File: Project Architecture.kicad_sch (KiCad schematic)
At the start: 0 parts

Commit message: First draft of schematic
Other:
- sheet Section A - Title A renamed SolarCharger
- sheet Section B - Title B renamed MCU
- added sheet Connectors (connectors.kicad_sch)
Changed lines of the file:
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@@
+	)
+	(sheet
+		(at 190.5 152.4)
+		(size 39.37 21.59)
+		(exclude_from_sim no)
+		(in_bom yes)
+		(on_board yes)
+		(dnp no)
+		(fields_autoplaced yes)
+		(stroke
+			(width 0.1524)
+			(type solid)
+		)
+		(fill
+			(color 0 0 0 0.0000)
+		)
+		(property "Sheetname" "Connectors"
+			(at 190.5 151.6884 0)
+			(effects
+				(font
+					(size 1.27 1.27)
+				)
+				(justify left bottom)
+			)
+		)
+		(property "Sheetfile" "connectors.kicad_sch"
+			(at 190.5 174.5746 0)
+			(effects
+				(font
+					(size 1.27 1.27)
+				)
+				(justify left top)
+			)
+		)
+		(instances
+			(project "solar_smart_station"
+				(path "/f9e05184-c88b-4a88-ae9c-ab2bdb32be7c/c5103ceb-5325-4a84-a025-9638a412984e"
+					(page "6")
+				)
+			)
+		)
 	)
 	(sheet
@@
 			(color 255 200 0 0.5020)
 		)
-		(property "Sheetname" "Section B - Title B"
+		(property "Sheetname" "MCU"
 			(at 190.5 113.2709 0)
 			(effects
@@
 			(color 128 255 128 0.5000)
 		)
-		(property "Sheetname" "Section A - Title A"
+		(property "Sheetname" "SolarCharger"
 			(at 190.5 75.1709 0)
 			(effects

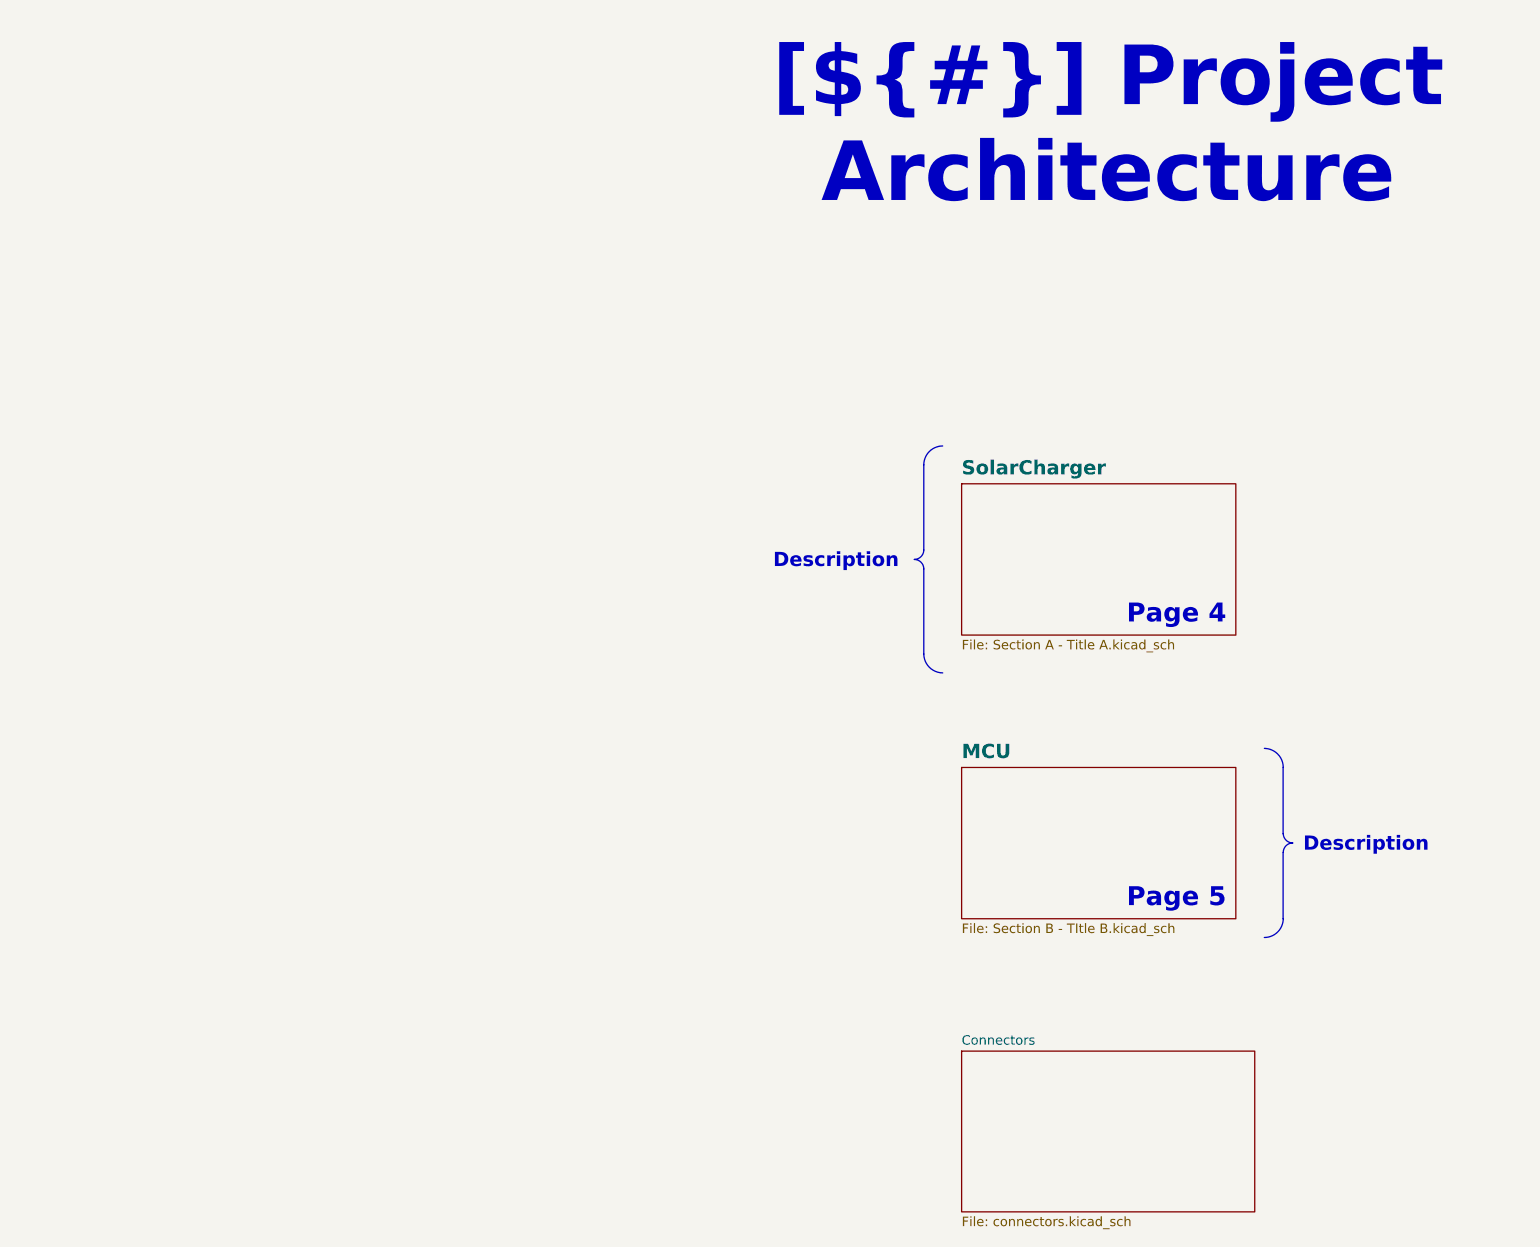
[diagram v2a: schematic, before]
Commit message: Add cell balancer - in progress
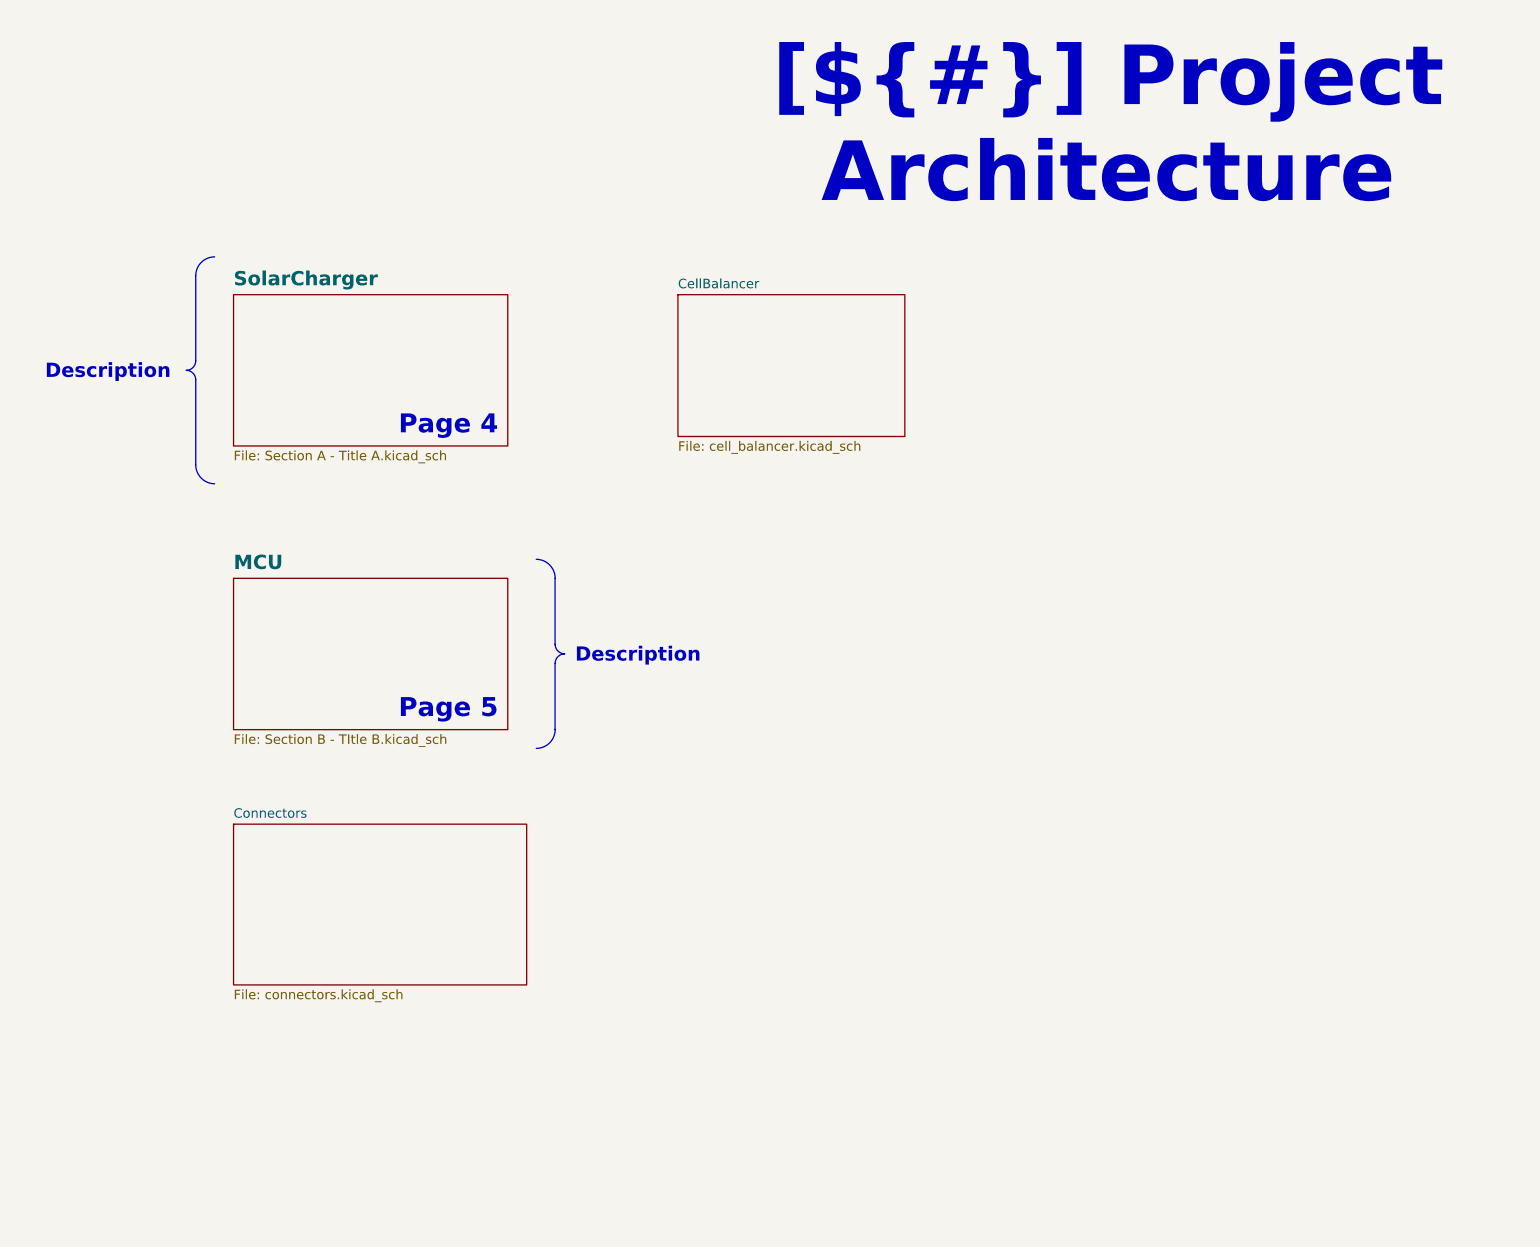
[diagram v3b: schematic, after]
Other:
- added sheet CellBalancer (cell_balancer.kicad_sch)
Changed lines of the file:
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@@
 	)
 	(arc
-		(start 185.42 85.09)
-		(mid 185.0451 85.9851)
-		(end 184.15 86.36)
-		(stroke
-			(width 0)
-			(type default)
-		)
-		(fill
-			(type none)
-		)
-	)
-	(arc
-		(start 234.97 124.44)
-		(mid 234.0749 124.0651)
-		(end 233.7 123.17)
-		(stroke
-			(width 0)
-			(type default)
-		)
-		(fill
-			(type none)
-		)
-	)
-	(arc
-		(start 233.7 125.71)
-		(mid 234.0749 124.8149)
-		(end 234.97 124.44)
-		(stroke
-			(width 0)
-			(type default)
-		)
-		(fill
-			(type none)
-		)
-	)
-	(arc
-		(start 233.7 134.6)
-		(mid 232.9561 136.3961)
-		(end 231.16 137.14)
-		(stroke
-			(width 0)
-			(type default)
-		)
-		(fill
-			(type none)
-		)
-	)
-	(arc
-		(start 184.15 86.36)
-		(mid 185.0451 86.7349)
-		(end 185.42 87.63)
-		(stroke
-			(width 0)
-			(type default)
-		)
-		(fill
-			(type none)
-		)
-	)
-	(arc
-		(start 187.96 101.6)
-		(mid 186.1698 100.8502)
-		(end 185.42 99.06)
-		(stroke
-			(width 0)
-			(type default)
-		)
-		(fill
-			(type none)
-		)
-	)
-	(arc
-		(start 231.16 111.74)
-		(mid 232.9502 112.4898)
-		(end 233.7 114.28)
-		(stroke
-			(width 0)
-			(type default)
-		)
-		(fill
-			(type none)
-		)
-	)
-	(arc
-		(start 185.42 73.66)
-		(mid 186.1639 71.8639)
-		(end 187.96 71.12)
+		(start 87.63 59.69)
+		(mid 87.2551 60.5851)
+		(end 86.36 60.96)
+		(stroke
+			(width 0)
+			(type default)
+		)
+		(fill
+			(type none)
+		)
+	)
+	(arc
+		(start 137.18 99.04)
+		(mid 136.2849 98.6651)
+		(end 135.91 97.77)
+		(stroke
+			(width 0)
+			(type default)
+		)
+		(fill
+			(type none)
+		)
+	)
+	(arc
+		(start 135.91 100.31)
+		(mid 136.2849 99.4149)
+		(end 137.18 99.04)
+		(stroke
+			(width 0)
+			(type default)
+		)
+		(fill
+			(type none)
+		)
+	)
+	(arc
+		(start 135.91 109.2)
+		(mid 135.1661 110.9961)
+		(end 133.37 111.74)
+		(stroke
+			(width 0)
+			(type default)
+		)
+		(fill
+			(type none)
+		)
+	)
+	(arc
+		(start 86.36 60.96)
+		(mid 87.2551 61.3349)
+		(end 87.63 62.23)
+		(stroke
+			(width 0)
+			(type default)
+		)
+		(fill
+			(type none)
+		)
+	)
+	(arc
+		(start 90.17 76.2)
+		(mid 88.3798 75.4502)
+		(end 87.63 73.66)
+		(stroke
+			(width 0)
+			(type default)
+		)
+		(fill
+			(type none)
+		)
+	)
+	(arc
+		(start 133.37 86.34)
+		(mid 135.1602 87.0898)
+		(end 135.91 88.88)
+		(stroke
+			(width 0)
+			(type default)
+		)
+		(fill
+			(type none)
+		)
+	)
+	(arc
+		(start 87.63 48.26)
+		(mid 88.3739 46.4639)
+		(end 90.17 45.72)
 		(stroke
 			(width 0)
@@
 	(text "Page 5"
 		(exclude_from_sim no)
-		(at 226.06 133.35 0)
+		(at 128.27 107.95 0)
 		(effects
 			(font
@@
 	(text "Page 4"
 		(exclude_from_sim no)
-		(at 226.06 95.25 0)
+		(at 128.27 69.85 0)
 		(effects
 			(font
@@
 	(text_box "Description"
 		(exclude_from_sim no)
-		(at 166.37 83.82 0)
+		(at 68.58 58.42 0)
 		(size 17.145 5.08)
 		(margins 1.4287 1.4287 1.4287 1.4287)
@@
 	(text_box "Description"
 		(exclude_from_sim no)
-		(at 234.95 121.92 0)
+		(at 137.16 96.52 0)
 		(size 26.015 5.1)
 		(margins 1.4287 1.4287 1.4287 1.4287)
@@
 	(polyline
 		(pts
-			(xy 185.42 87.63) (xy 185.42 99.06)
+			(xy 87.63 62.23) (xy 87.63 73.66)
 		)
 		(stroke
@@
 	(polyline
 		(pts
-			(xy 233.68 125.73) (xy 233.68 134.62)
+			(xy 135.89 100.33) (xy 135.89 109.22)
 		)
 		(stroke
@@
 	(polyline
 		(pts
-			(xy 185.42 85.09) (xy 185.42 73.66)
+			(xy 87.63 59.69) (xy 87.63 48.26)
 		)
 		(stroke
@@
 	(polyline
 		(pts
-			(xy 233.68 114.3) (xy 233.68 123.19)
+			(xy 135.89 88.9) (xy 135.89 97.79)
 		)
 		(stroke
@@
 	)
 	(sheet
-		(at 190.5 152.4)
-		(size 39.37 21.59)
+		(at 152.4 50.8)
+		(size 30.48 19.05)
 		(exclude_from_sim no)
 		(in_bom yes)
@@
 		)
 		(fill
-			(color 0 0 0 0.0000)
-		)
-		(property "Sheetname" "Connectors"
-			(at 190.5 151.6884 0)
+			(color 85 146 255 1.0000)
+		)
+		(property "Sheetname" "CellBalancer"
+			(at 152.4 50.0884 0)
 			(effects
 				(font
@@
 			)
 		)
-		(property "Sheetfile" "connectors.kicad_sch"
-			(at 190.5 174.5746 0)
+		(property "Sheetfile" "cell_balancer.kicad_sch"
+			(at 152.4 70.4346 0)
 			(effects
 				(font
@@
 	)
 	(sheet
-		(at 190.5 114.3)
-		(size 36.83 20.32)
+		(at 92.71 121.92)
+		(size 39.37 21.59)
 		(exclude_from_sim no)
 		(in_bom yes)
@@
 		)
 		(fill
+			(color 0 0 0 0.0000)
+		)
+		(property "Sheetname" "Connectors"
+			(at 92.71 121.2084 0)
+			(effects
+				(font
+					(size 1.27 1.27)
+				)
+				(justify left bottom)
+			)
+		)
+		(property "Sheetfile" "connectors.kicad_sch"
+			(at 92.71 144.0946 0)
+			(effects
+				(font
+					(size 1.27 1.27)
+				)
+				(justify left top)
+			)
+		)
+		(instances
+			(project "solar_smart_station"
+				(path "/f9e05184-c88b-4a88-ae9c-ab2bdb32be7c/c5103ceb-5325-4a84-a025-9638a412984e"
+					(page "7")
+				)
+			)
+		)
+	)
+	(sheet
+		(at 92.71 88.9)
+		(size 36.83 20.32)
+		(exclude_from_sim no)
+		(in_bom yes)
+		(on_board yes)
+		(dnp no)
+		(fields_autoplaced yes)
+		(stroke
+			(width 0.1524)
+			(type solid)
+		)
+		(fill
 			(color 255 200 0 0.5020)
 		)
 		(property "Sheetname" "MCU"
-			(at 190.5 113.2709 0)
+			(at 92.71 87.8709 0)
 			(effects
 				(font
@@
 		)
 		(property "Sheetfile" "Section B - TItle B.kicad_sch"
-			(at 190.5 135.2046 0)
+			(at 92.71 109.8046 0)
 			(effects
 				(font
@@
 	)
 	(sheet
-		(at 190.5 76.2)
+		(at 92.71 50.8)
 		(size 36.83 20.32)
 		(exclude_from_sim no)
@@
 		)
 		(property "Sheetname" "SolarCharger"
-			(at 190.5 75.1709 0)
+			(at 92.71 49.7709 0)
 			(effects
 				(font
@@
 		)
 		(property "Sheetfile" "Section A - Title A.kicad_sch"
-			(at 190.5 97.1046 0)
-			(effects
-				(font
+			(at 92.71 71.7046 0)
+			(effects
+				(font

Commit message: Finish checking - Ready for 1st release
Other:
- note added: "Page 6"
- note added: "Page 7"
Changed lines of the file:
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@@
+		)
+	)
+	(text "Page 6"
+		(exclude_from_sim no)
+		(at 205.994 67.818 0)
+		(effects
+			(font
+				(size 2.54 2.54)
+				(bold yes)
+				(color 20 60 40 1)
+			)
+			(justify right bottom)
+			(href "#6")
+		)
+	)
+	(text "Page 7"
+		(exclude_from_sim no)
+		(at 207.772 108.458 0)
+		(effects
+			(font
+				(size 2.54 2.54)
+				(bold yes)
+				(color 20 60 40 1)
+			)
+			(justify right bottom)
+			(href "#7")
 		)
 	)
@@
 	)
 	(sheet
-		(at 152.4 50.8)
+		(at 177.8 50.8)
 		(size 30.48 19.05)
 		(exclude_from_sim no)
@@
 		)
 		(property "Sheetname" "CellBalancer"
-			(at 152.4 50.0884 0)
+			(at 177.8 50.0884 0)
 			(effects
 				(font
@@
 		)
 		(property "Sheetfile" "cell_balancer.kicad_sch"
-			(at 152.4 70.4346 0)
+			(at 177.8 70.4346 0)
 			(effects
 				(font
@@
 	)
 	(sheet
-		(at 92.71 121.92)
+		(at 172.72 90.17)
 		(size 39.37 21.59)
 		(exclude_from_sim no)
@@
 		)
 		(fill
-			(color 0 0 0 0.0000)
+			(color 138 255 32 1.0000)
 		)
 		(property "Sheetname" "Connectors"
-			(at 92.71 121.2084 0)
+			(at 172.72 89.4584 0)
 			(effects
 				(font
@@
 		)
 		(property "Sheetfile" "connectors.kicad_sch"
-			(at 92.71 144.0946 0)
-			(effects
-				(font
+			(at 172.72 112.3446 0)
+			(effects
+				(font
